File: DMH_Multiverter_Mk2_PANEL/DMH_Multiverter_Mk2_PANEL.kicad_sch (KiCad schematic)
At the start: 29 parts, among them J0 Panel_GND_Solder_Wire_Pad

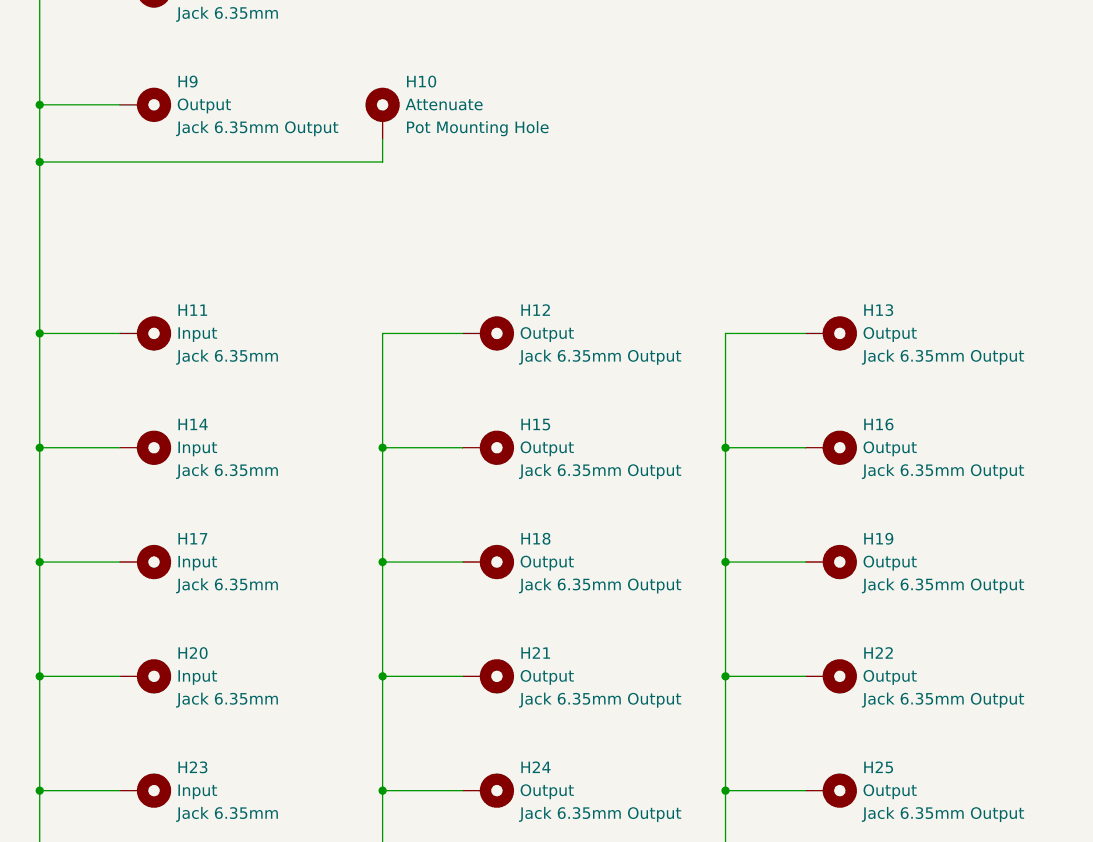
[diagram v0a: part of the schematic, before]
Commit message: Added 3rd attenuverter to Panel and Schematic
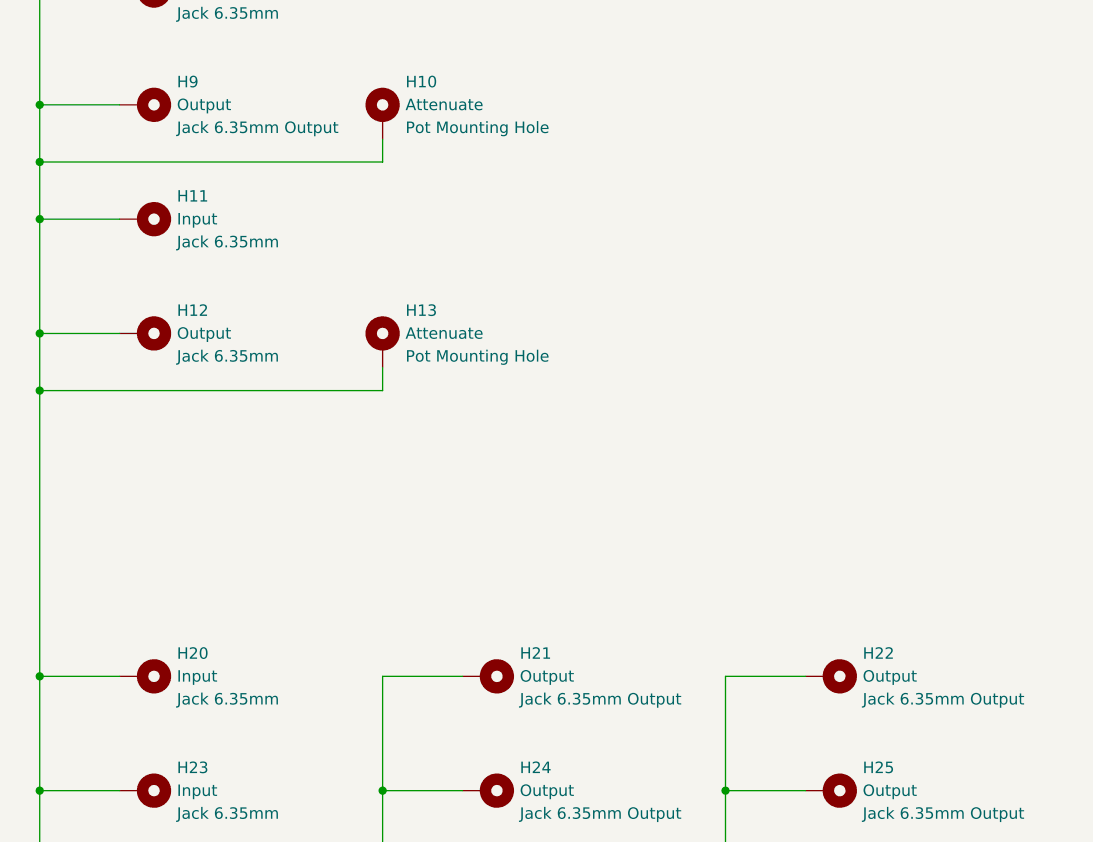
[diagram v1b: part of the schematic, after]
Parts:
- removed H12, H13, H15, H16, H18, H19: Output, SynthStuff:Jack_6.35mm_Cutout_Output_v6, symbol SynthStuff:MountingHole_Jack6.35mm_Output_v2
- removed H17: Input, SynthStuff:Jack_6.35mm_Cutout_v3, symbol SynthStuff:MountingHole_Jack6.35mm_v2
- added H13: Attenuate, SynthStuff:Pot_Cutout_Small_attv_P110KH1, symbol SynthStuff:MountingHole_Pot
- H12: renamed from H14; value Input -> Output; footprint SynthStuff:Jack_6.35mm_Cutout_v3 -> SynthStuff:Jack_6.35mm_Cutout_Output_v6
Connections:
- net GND: now also H13.1
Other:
- moved on the sheet: H11, H12
